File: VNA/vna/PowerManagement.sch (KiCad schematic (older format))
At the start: 5 parts, among them U6 LM1117-5.0

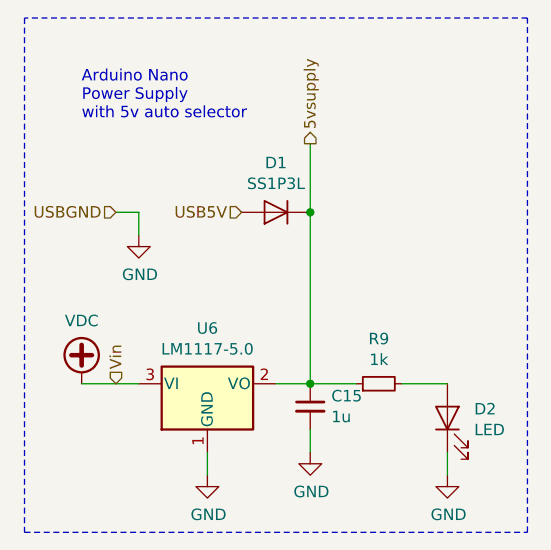
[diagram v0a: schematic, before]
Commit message: custom footprint for couplers, added decoupling caps
added custom footprint for directional couplers - will need to verify it

added decoupling caps to ad9851
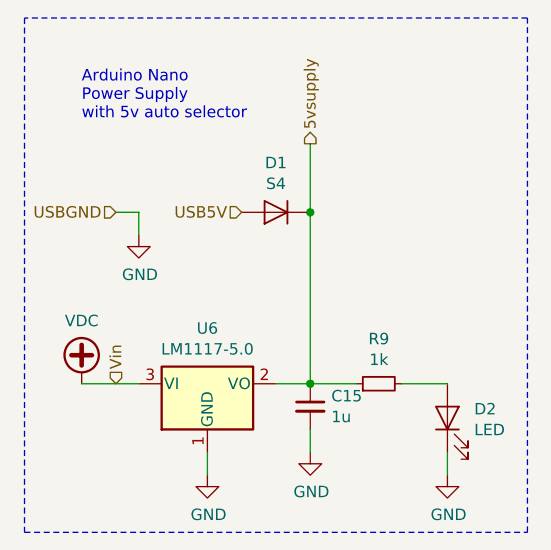
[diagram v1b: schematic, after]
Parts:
- C15: footprint Capacitor_SMD:C_0805_2012Metric_Pad1.15x1.40mm_HandSolder -> Capacitor_SMD:C_1206_3216Metric_Pad1.42x1.75mm_HandSolder
- D1: value SS1P3L -> S4; footprint (none) -> Diode_SMD:D_SOD-123
- R9: footprint Resistor_SMD:R_0805_2012Metric_Pad1.15x1.40mm_HandSolder -> Resistor_SMD:R_1206_3216Metric_Pad1.42x1.75mm_HandSolder
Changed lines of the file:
@@
 $Descr A4 11693 8268
 encoding utf-8
-Sheet 7 10
+Sheet 6 10
 Title ""
 Date ""
@@
 P 3250 2000
 F 0 "D1" H 3250 1784 50  0000 C CNN
-F 1 "SS1P3L" H 3250 1875 50  0000 C CNN
-F 2 "" H 3250 2000 50  0001 C CNN
+F 1 "S4" H 3250 1875 50  0000 C CNN
+F 2 "Diode_SMD:D_SOD-123" H 3250 2000 50  0001 C CNN
 F 3 "~" H 3250 2000 50  0001 C CNN
 	1    3250 2000
@@
 F 0 "R9" V 3896 2750 50  0000 C CNN
 F 1 "1k" V 3805 2750 50  0000 C CNN
-F 2 "Resistor_SMD:R_0805_2012Metric_Pad1.15x1.40mm_HandSolder" H 3700 2750 50  0001 C CNN
+F 2 "Resistor_SMD:R_1206_3216Metric_Pad1.42x1.75mm_HandSolder" H 3700 2750 50  0001 C CNN
 F 3 "~" H 3700 2750 50  0001 C CNN
 	1    3700 2750
@@
 F 0 "C15" H 3492 2896 50  0000 L CNN
 F 1 "1u" H 3492 2805 50  0000 L CNN
-F 2 "Capacitor_SMD:C_0805_2012Metric_Pad1.15x1.40mm_HandSolder" H 3400 2850 50  0001 C CNN
+F 2 "Capacitor_SMD:C_1206_3216Metric_Pad1.42x1.75mm_HandSolder" H 3400 2850 50  0001 C CNN
 F 3 "~" H 3400 2850 50  0001 C CNN
 	1    3400 2850

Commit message: initial pcb design
initial layout and grouping of components complete
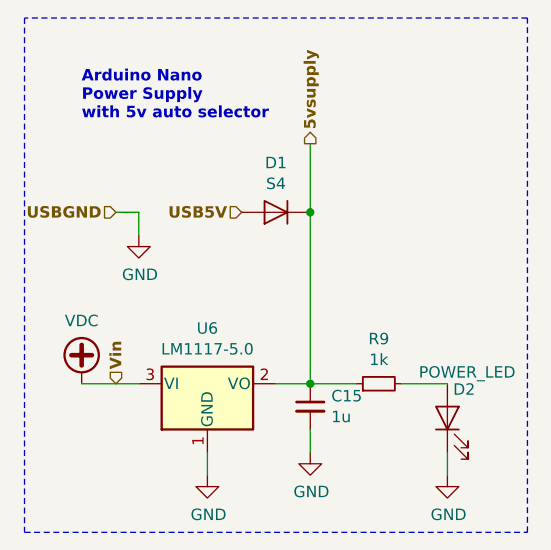
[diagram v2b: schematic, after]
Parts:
- C15: footprint Capacitor_SMD:C_1206_3216Metric_Pad1.42x1.75mm_HandSolder -> Capacitor_SMD:C_0805_2012Metric_Pad1.15x1.40mm_HandSolder
- D2: value LED -> POWER_LED
- R9: footprint Resistor_SMD:R_1206_3216Metric_Pad1.42x1.75mm_HandSolder -> Resistor_SMD:R_0805_2012Metric_Pad1.15x1.40mm_HandSolder
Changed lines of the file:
@@
 encoding utf-8
 Sheet 6 10
-Title ""
-Date ""
-Rev ""
-Comp ""
+Title "Power Management"
+Date "2019-09-25"
+Rev "0.1"
+Comp "Benjamin Jackson"
 Comment1 ""
 Comment2 ""
@@
 Comment4 ""
 $EndDescr
-Text HLabel 3100 2000 0    50   Input ~ 0
+Text HLabel 3100 2000 0    50   Input ~ 10
 USB5V
-Text HLabel 2550 2000 0    50   Input ~ 0
+Text HLabel 2550 2000 0    50   Input ~ 10
 USBGND
-Text HLabel 3400 1700 1    50   Output ~ 0
+Text HLabel 3400 1700 1    50   Output ~ 10
 5vsupply
 Wire Wire Line
@@
 Wire Wire Line
 	2400 2750 2650 2750
-Text Notes 2400 1600 0    50   ~ 0
+Text Notes 2400 1600 0    50   ~ 10
 Arduino Nano \nPower Supply\nwith 5v auto selector
 Wire Wire Line
@@
 U 1 1 5DCF519B
 P 4000 2900
-F 0 "D2" V 4039 2783 50  0000 R CNN
-F 1 "LED" V 3948 2783 50  0000 R CNN
+F 0 "D2" V 4125 2875 50  0000 R CNN
+F 1 "POWER_LED" V 4200 3025 50  0000 R CNN
 F 2 "LED_SMD:LED_0805_2012Metric" H 4000 2900 50  0001 C CNN
 F 3 "~" H 4000 2900 50  0001 C CNN
@@
 F 0 "R9" V 3896 2750 50  0000 C CNN
 F 1 "1k" V 3805 2750 50  0000 C CNN
-F 2 "Resistor_SMD:R_1206_3216Metric_Pad1.42x1.75mm_HandSolder" H 3700 2750 50  0001 C CNN
+F 2 "Resistor_SMD:R_0805_2012Metric_Pad1.15x1.40mm_HandSolder" H 3700 2750 50  0001 C CNN
 F 3 "~" H 3700 2750 50  0001 C CNN
 	1    3700 2750
@@
 	1    0    0    -1
 $EndComp
-Text HLabel 2550 2750 1    50   Input ~ 0
+Text HLabel 2550 2750 1    50   Input ~ 10
 Vin
 $Comp
@@
 F 0 "C15" H 3492 2896 50  0000 L CNN
 F 1 "1u" H 3492 2805 50  0000 L CNN
-F 2 "Capacitor_SMD:C_1206_3216Metric_Pad1.42x1.75mm_HandSolder" H 3400 2850 50  0001 C CNN
+F 2 "Capacitor_SMD:C_0805_2012Metric_Pad1.15x1.40mm_HandSolder" H 3400 2850 50  0001 C CNN
 F 3 "~" H 3400 2850 50  0001 C CNN
 	1    3400 2850
